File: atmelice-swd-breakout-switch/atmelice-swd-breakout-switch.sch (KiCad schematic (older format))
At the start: 3 parts, among them J1 Conn_02x05_Odd_Even, J2 Conn_01x06, SW1 SW_DPDT_x2

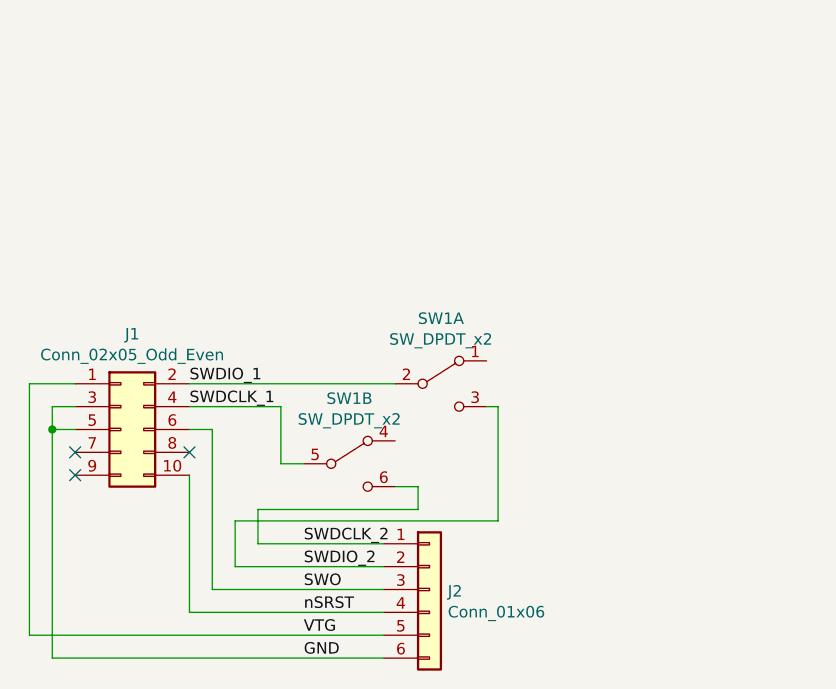
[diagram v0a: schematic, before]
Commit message: atmelice-swd-breakout-switch: add AVR connector (2021Jan rev)
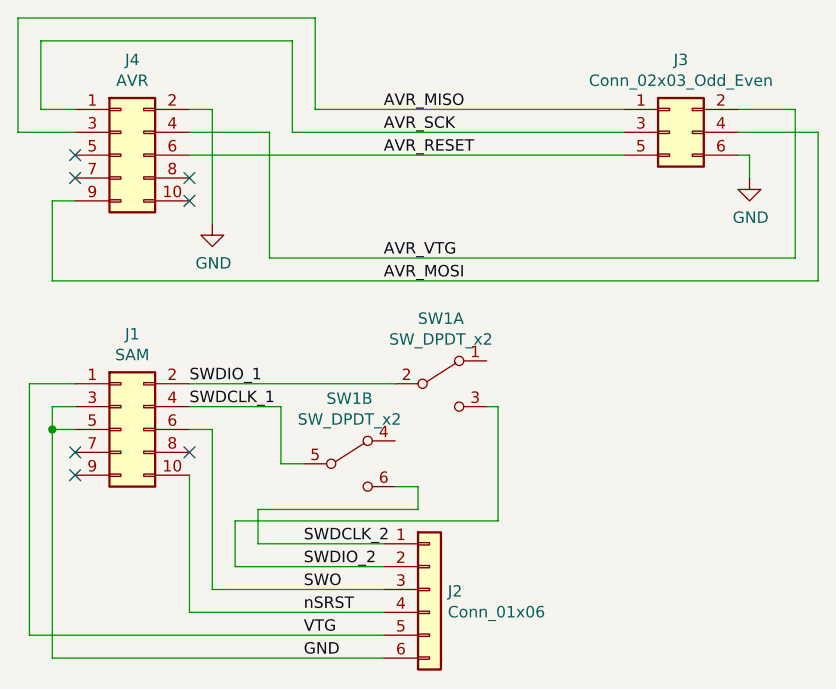
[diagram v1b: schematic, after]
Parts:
- added J3: Conn_02x03_Odd_Even, tom-connectors:PinHeader_2x03_P2.54mm_Vertical, symbol tom-connectors:Conn_02x03_Odd_Even
- added J4: AVR, tom-connectors:PinSocket_2x05_P1.27mm_Vertical, symbol tom-connectors:Conn_02x05_Odd_Even
- J1: value Conn_02x05_Odd_Even -> SAM
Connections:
- net GND: now also J3.6 (Pin_6), J4.2 (Pin_2)
- new net AVR_MISO: J3.1 (Pin_1), J4.3 (Pin_3)
- new net AVR_MOSI: J3.4 (Pin_4), J4.9 (Pin_9)
- new net AVR_RESET: J3.5 (Pin_5), J4.6 (Pin_6)
- new net AVR_SCK: J3.3 (Pin_3), J4.1 (Pin_1)
- new net AVR_VTG: J3.2 (Pin_2), J4.4 (Pin_4)
- no-connect marks 3 -> 7
